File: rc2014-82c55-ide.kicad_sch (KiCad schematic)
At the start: 22 parts, among them J1 Conn_01x02, J2 Conn_02x20_Odd_Even, J3 Conn_02x22_Odd_Even, J5 Conn_01x02, P1 Conn_01x39, SW1 SW_DIP_x06, U1 82C55A_PLCC, U2 74HCT688, U3 74HCT04

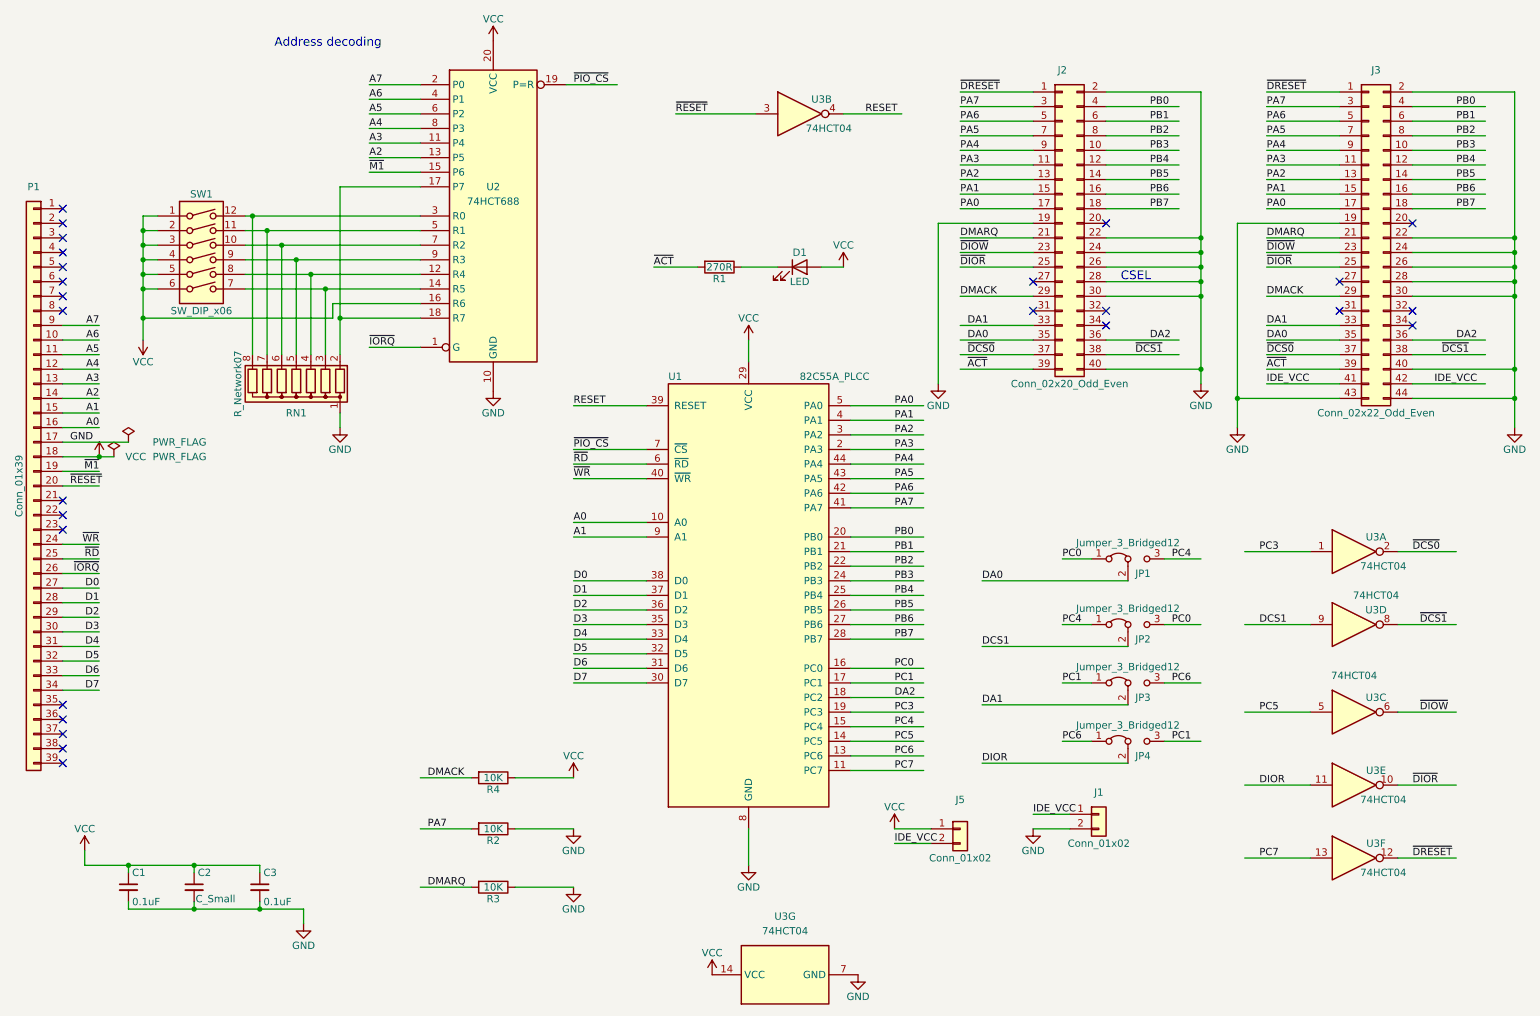
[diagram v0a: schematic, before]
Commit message: update to kicad 9
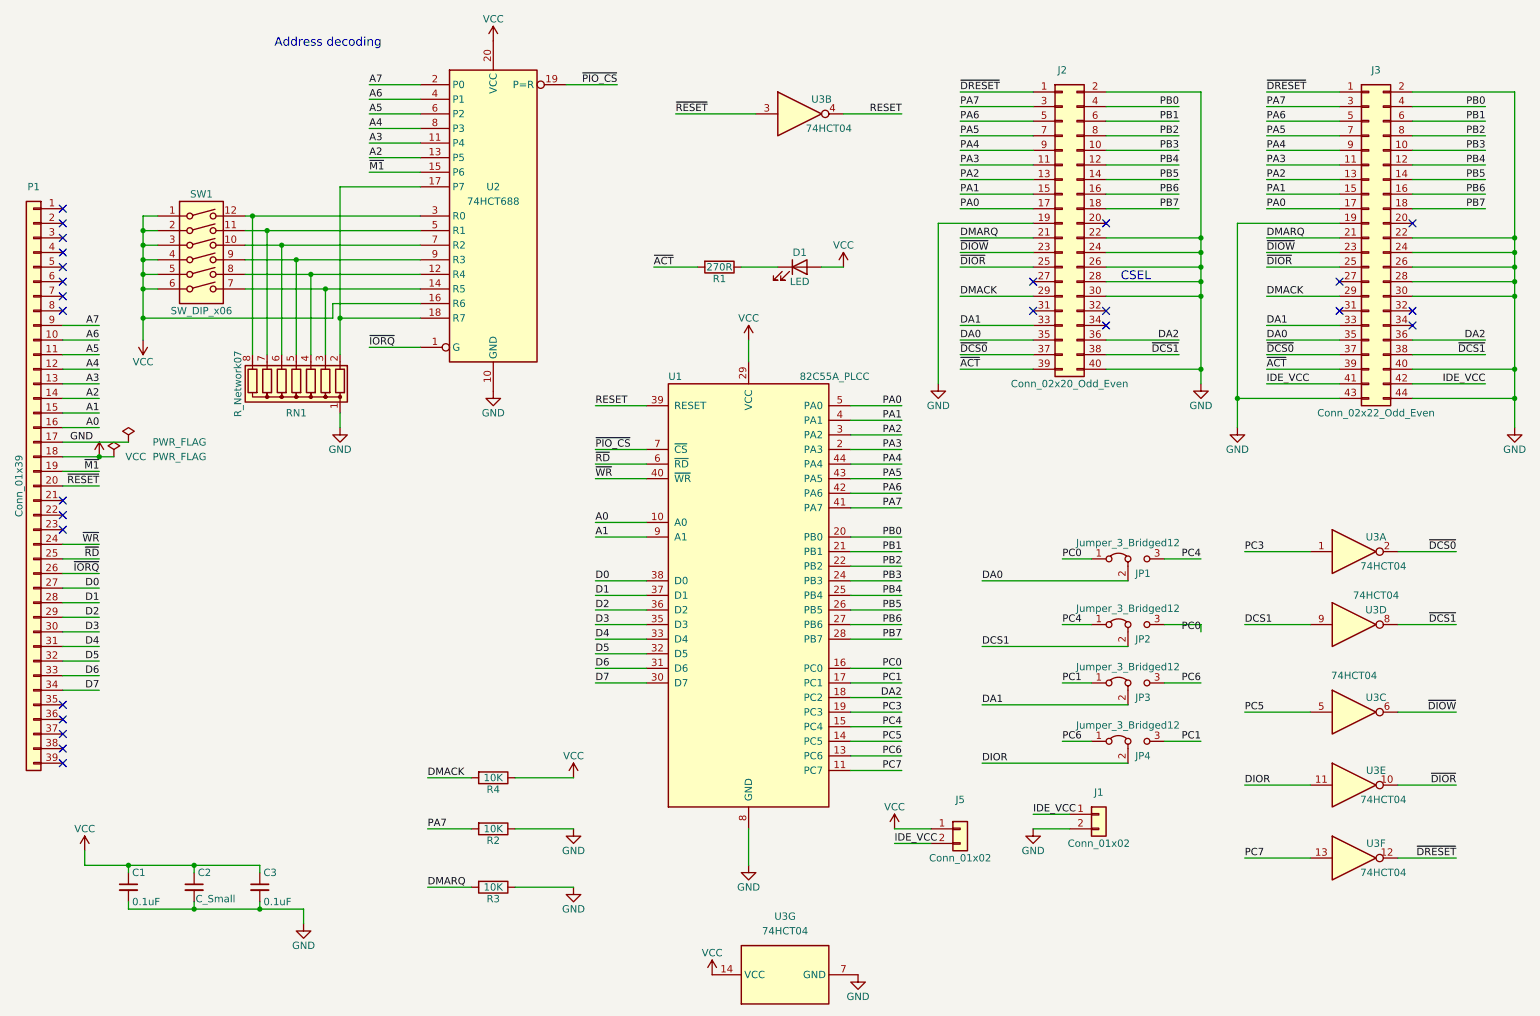
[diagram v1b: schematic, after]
